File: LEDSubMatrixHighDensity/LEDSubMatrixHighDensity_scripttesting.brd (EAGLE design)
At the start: 16.9 x 127 mm, 129 parts, among them IC1 TLC5955DCAR, IC2 TLC5955DCAR, IC3 TLC5955DCAR, IC4 TLC5955DCAR, IC5 TLC5955DCAR, IC6 TLC5955DCAR, IC7 TLC5955DCAR, IC8 TLC5955DCAR

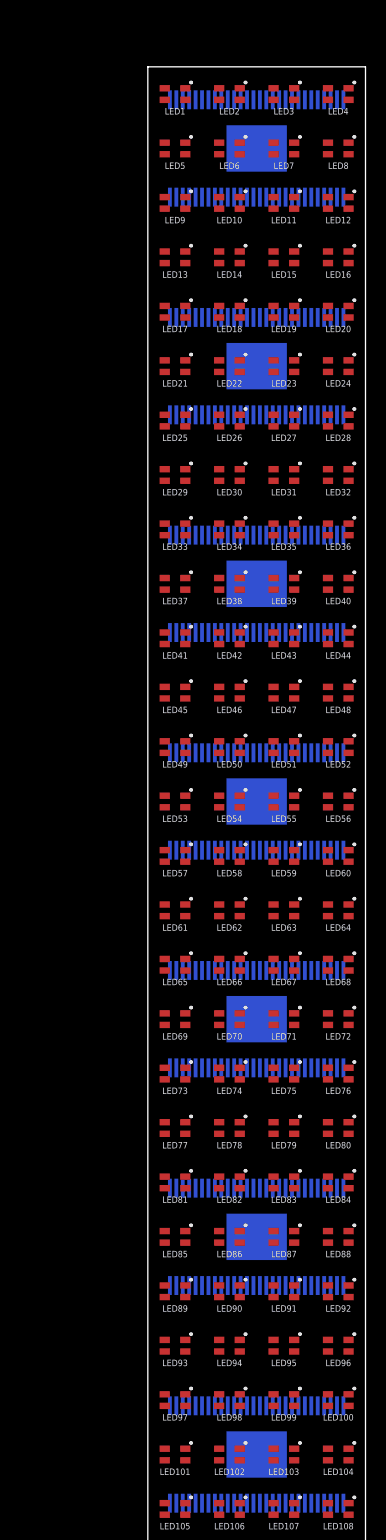
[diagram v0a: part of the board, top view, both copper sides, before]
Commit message: Automated Python scripts and one block of LED matrix
Added a bunch of python scripts for automating Eagle design. Created a template for one LED driver block of board (to be copied later)
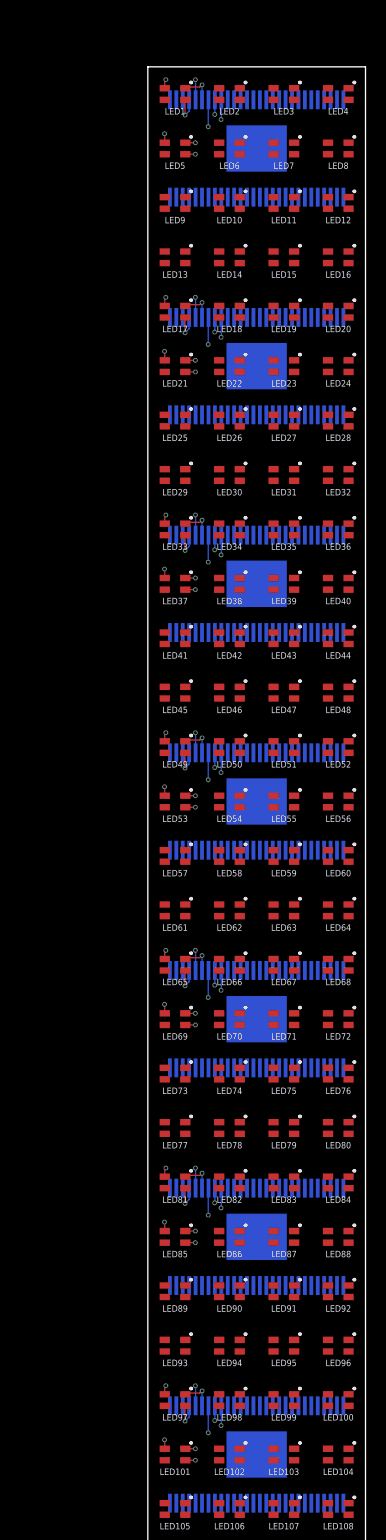
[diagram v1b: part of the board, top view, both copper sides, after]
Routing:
- net N$LEDR69_IC5_PIN8: track 0.00 -> 6.38 mm, vias 0 -> 2
- net N$LEDR37_IC3_PIN8: track 0.00 -> 6.38 mm, vias 0 -> 2
- net N$LEDR21_IC2_PIN8: track 0.00 -> 6.38 mm, vias 0 -> 2
- net N$LEDR5_IC1_PIN8: track 0.00 -> 6.38 mm, vias 0 -> 2
- net N$LEDR53_IC4_PIN8: track 0.00 -> 6.38 mm, vias 0 -> 2
- net N$LEDR85_IC6_PIN8: track 0.00 -> 6.38 mm, vias 0 -> 2
- net N$LEDR101_IC7_PIN8: track 0.00 -> 6.38 mm, vias 0 -> 2
- net N$LEDG69_IC5_PIN9: track 0.00 -> 5.87 mm, vias 0 -> 2
- net N$LEDG37_IC3_PIN9: track 0.00 -> 5.87 mm, vias 0 -> 2
- net N$LEDG21_IC2_PIN9: track 0.00 -> 5.87 mm, vias 0 -> 2
- net N$LEDG5_IC1_PIN9: track 0.00 -> 5.87 mm, vias 0 -> 2
- net N$LEDG53_IC4_PIN9: track 0.00 -> 5.87 mm, vias 0 -> 2
- net N$LEDG85_IC6_PIN9: track 0.00 -> 5.87 mm, vias 0 -> 2
- net N$LEDG101_IC7_PIN9: track 0.00 -> 5.87 mm, vias 0 -> 2
- net N$LEDB5_IC1_PIN7: track 0.00 -> 5.44 mm, vias 0 -> 2
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
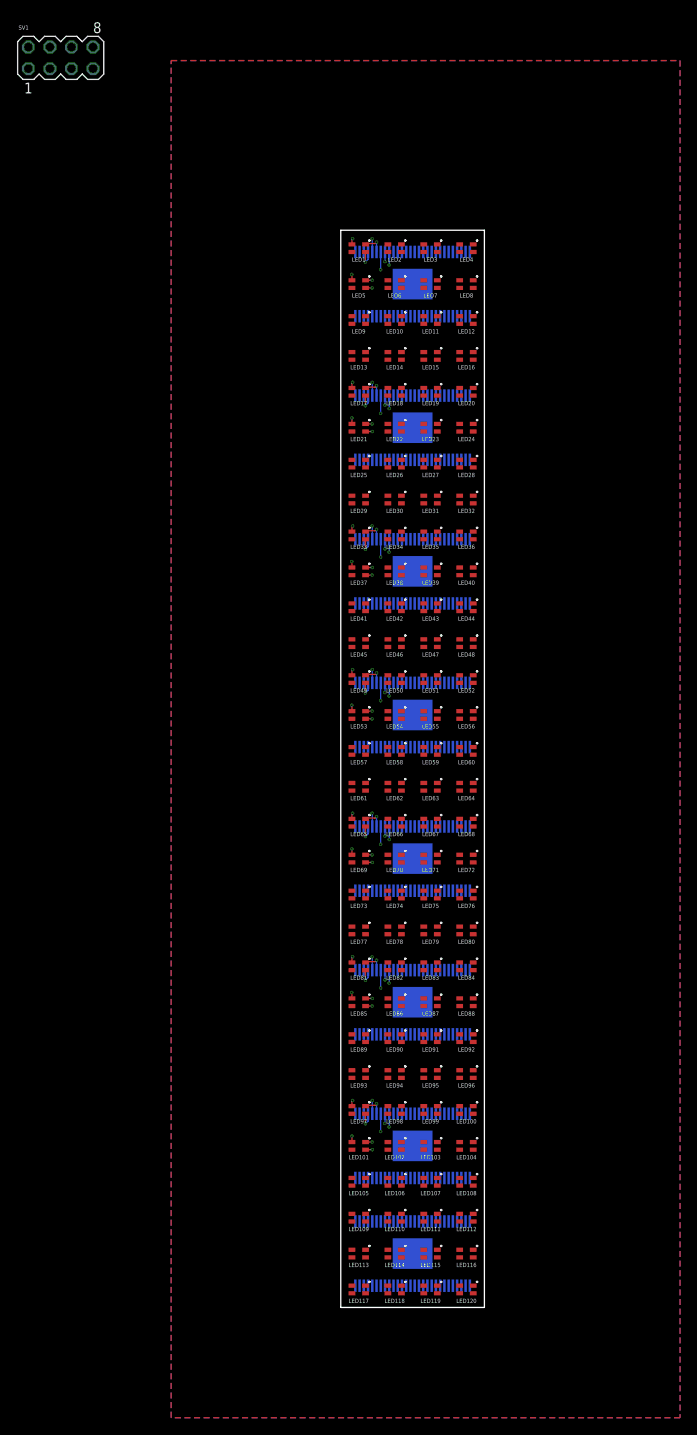
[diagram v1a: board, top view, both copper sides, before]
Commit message: added pictures of led matrix pcbs
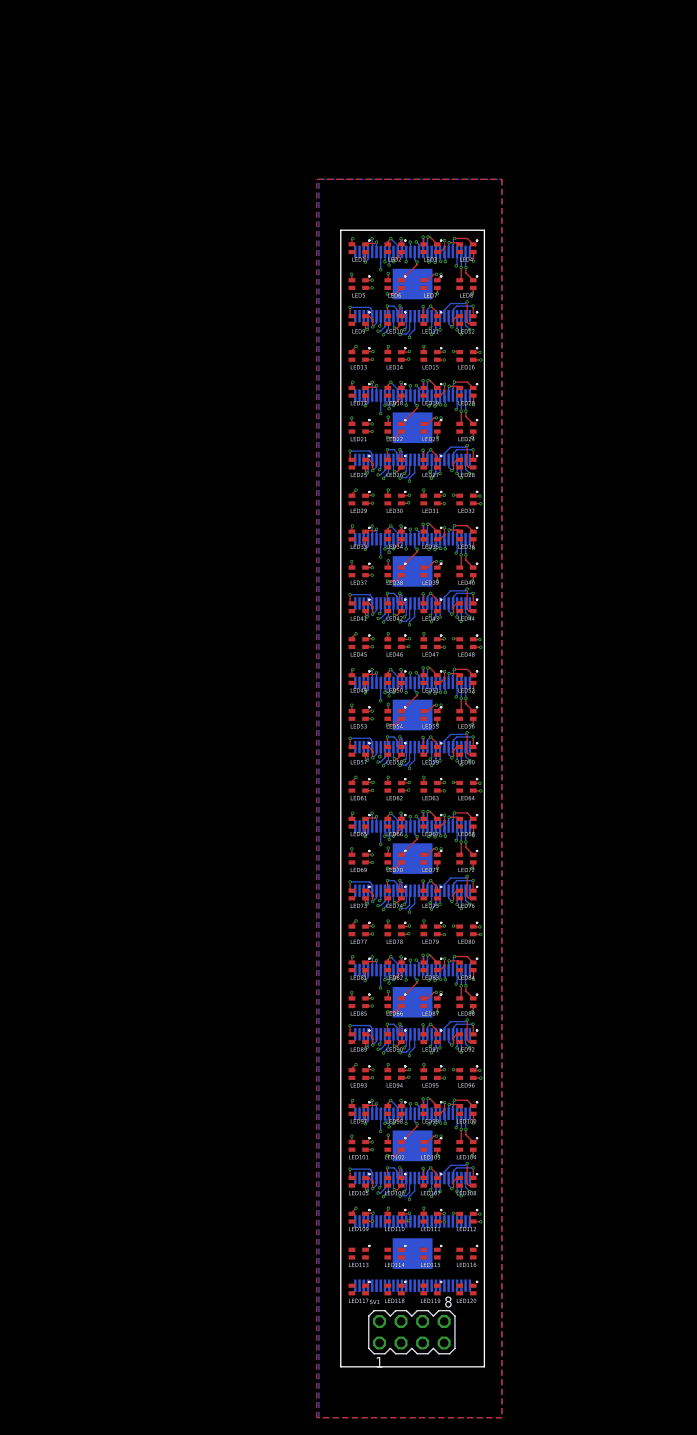
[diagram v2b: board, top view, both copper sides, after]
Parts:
- moved SV1 155.8 mm to (8.38, -129.9)
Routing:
- net N$LEDB96_IC6_PIN32: track 0.00 -> 8.16 mm, vias 0 -> 2
- net N$LEDB112_IC7_PIN32: track 0.00 -> 8.16 mm, vias 0 -> 2
- net N$LEDB48_IC3_PIN32: track 0.00 -> 8.16 mm, vias 0 -> 2
- net N$LEDB16_IC1_PIN32: track 0.00 -> 8.16 mm, vias 0 -> 2
- net N$LEDB32_IC2_PIN32: track 0.00 -> 8.16 mm, vias 0 -> 2
- net N$LEDB64_IC4_PIN32: track 0.00 -> 8.16 mm, vias 0 -> 2
- net N$LEDB80_IC5_PIN32: track 0.00 -> 8.16 mm, vias 0 -> 2
- net N$LEDB70_IC5_PIN13: track 0.00 -> 7.80 mm, vias 0 -> 2
- net N$LEDB22_IC2_PIN13: track 0.00 -> 7.80 mm, vias 0 -> 2
- net N$LEDB6_IC1_PIN13: track 0.00 -> 7.80 mm, vias 0 -> 2
- net N$LEDB54_IC4_PIN13: track 0.00 -> 7.80 mm, vias 0 -> 2
- net N$LEDB38_IC3_PIN13: track 0.00 -> 7.80 mm, vias 0 -> 2
- net N$LEDB102_IC7_PIN13: track 0.00 -> 7.80 mm, vias 0 -> 2
- net N$LEDB86_IC6_PIN13: track 0.00 -> 7.80 mm, vias 0 -> 2
- net N$LEDB29_IC2_PIN50: track 0.00 -> 7.30 mm, vias 0 -> 2
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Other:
- board size 16.9 x 127 mm -> 16.9 x 134 mm

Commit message: Finished placing all LEDs and Led Drivers
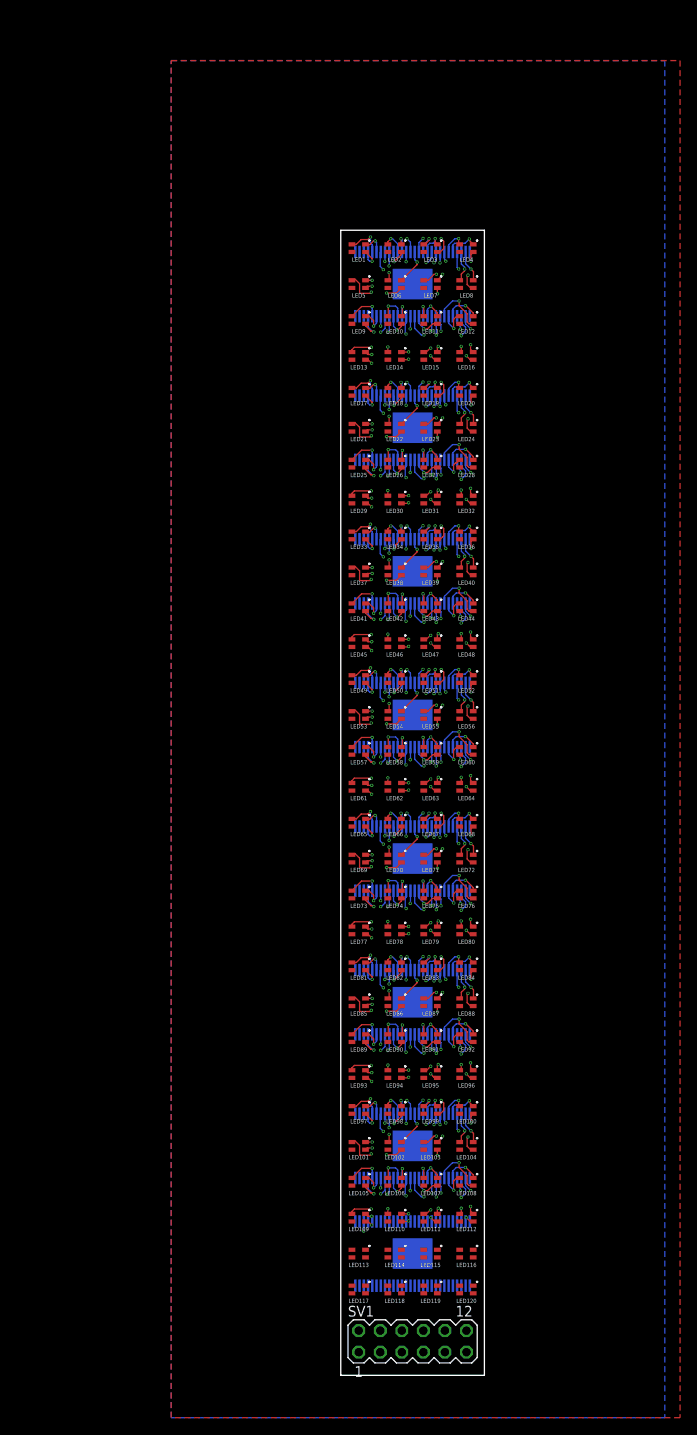
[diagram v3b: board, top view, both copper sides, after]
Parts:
- SV1: device con-lstb:MA04-2 -> con-lstb:MA06-2
- moved SV1 1.08 mm to (8.47, -131.0)
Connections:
- removed net SIN_MCU: IC1.1, IC2.1, IC3.1, IC4.1, IC5.1, IC6.1, IC7.1, IC8.1, SV1.8
- new net N$9: SV1.5
- new net SIN_1,2: IC1.1, IC2.1
- new net SIN_3,4: IC3.1, IC4.1
- new net SIN_5,6: IC5.1, IC6.1
- new net SIN_7,8: IC7.1, IC8.1
- new net SOUT2: IC2.28
- new net SOUT3: IC3.28
- new net SOUT4: IC4.28
- new net SOUT5: IC5.28
- new net SOUT6: IC6.28
- new net SOUT7: IC7.28
- new net SOUT8: IC8.28
- net 3V3: now also SV1.10, SV1.9; no longer SV1.4
- net GND: now also SV1.11, SV1.12; no longer SV1.2
- net GSCLK: now also SV1.6; no longer SV1.5
- net LAT: now also SV1.4, SV1.8
- net SCLK: now also SV1.2, SV1.7; no longer SV1.6
- net SOUT1: no longer IC2.28, IC3.28, IC4.28, IC5.28, IC6.28, IC7.28, IC8.28, SV1.7
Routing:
- net LAT: track 0.00 -> 15.8 mm, vias 0 -> 1
- net N$LEDB27_IC2_PIN41: track 0.00 -> 3.57 mm, vias 0 -> 1
- net N$LEDB75_IC5_PIN41: track 0.00 -> 3.57 mm, vias 0 -> 1
- net N$LEDB59_IC4_PIN41: track 0.00 -> 3.57 mm, vias 0 -> 1
- net N$LEDB43_IC3_PIN41: track 0.00 -> 3.57 mm, vias 0 -> 1
- net N$LEDB91_IC6_PIN41: track 0.00 -> 3.57 mm, vias 0 -> 1
- net N$LEDB107_IC7_PIN41: track 0.00 -> 3.57 mm, vias 0 -> 1
- net N$LEDB11_IC1_PIN41: track 0.00 -> 3.57 mm, vias 0 -> 1
- net N$LEDR85_IC6_PIN8: track 6.38 -> 9.85 mm
- net N$LEDR53_IC4_PIN8: track 6.38 -> 9.85 mm
- net N$LEDR101_IC7_PIN8: track 6.38 -> 9.85 mm
- net N$LEDR69_IC5_PIN8: track 6.38 -> 9.85 mm
- net N$LEDR37_IC3_PIN8: track 6.38 -> 9.85 mm
- net N$LEDR21_IC2_PIN8: track 6.38 -> 9.85 mm
- net N$LEDR5_IC1_PIN8: track 6.38 -> 9.85 mm
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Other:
- board size 16.9 x 134 mm -> 16.9 x 135 mm
